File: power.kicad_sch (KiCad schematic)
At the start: 33 parts, among them J5 Conn_01x02, Q1 2N7002K, Q2 CSD17311Q5, Q3 CSD17311Q5, U10 DS4432U+, U13 TPS40305, U9 INA260

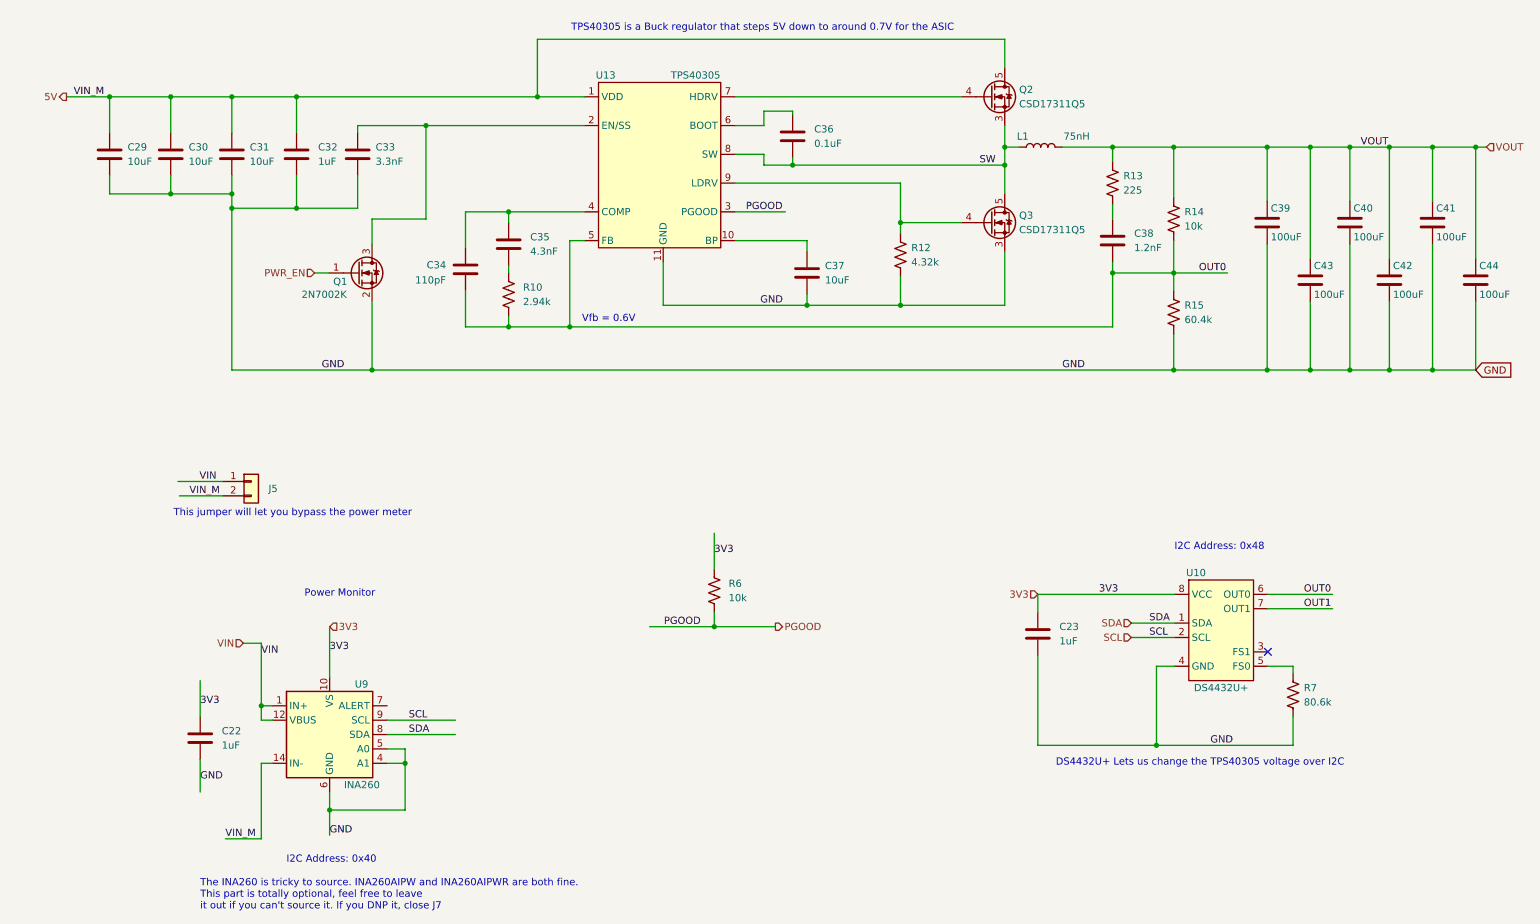
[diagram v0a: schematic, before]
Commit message: adding logo and docs
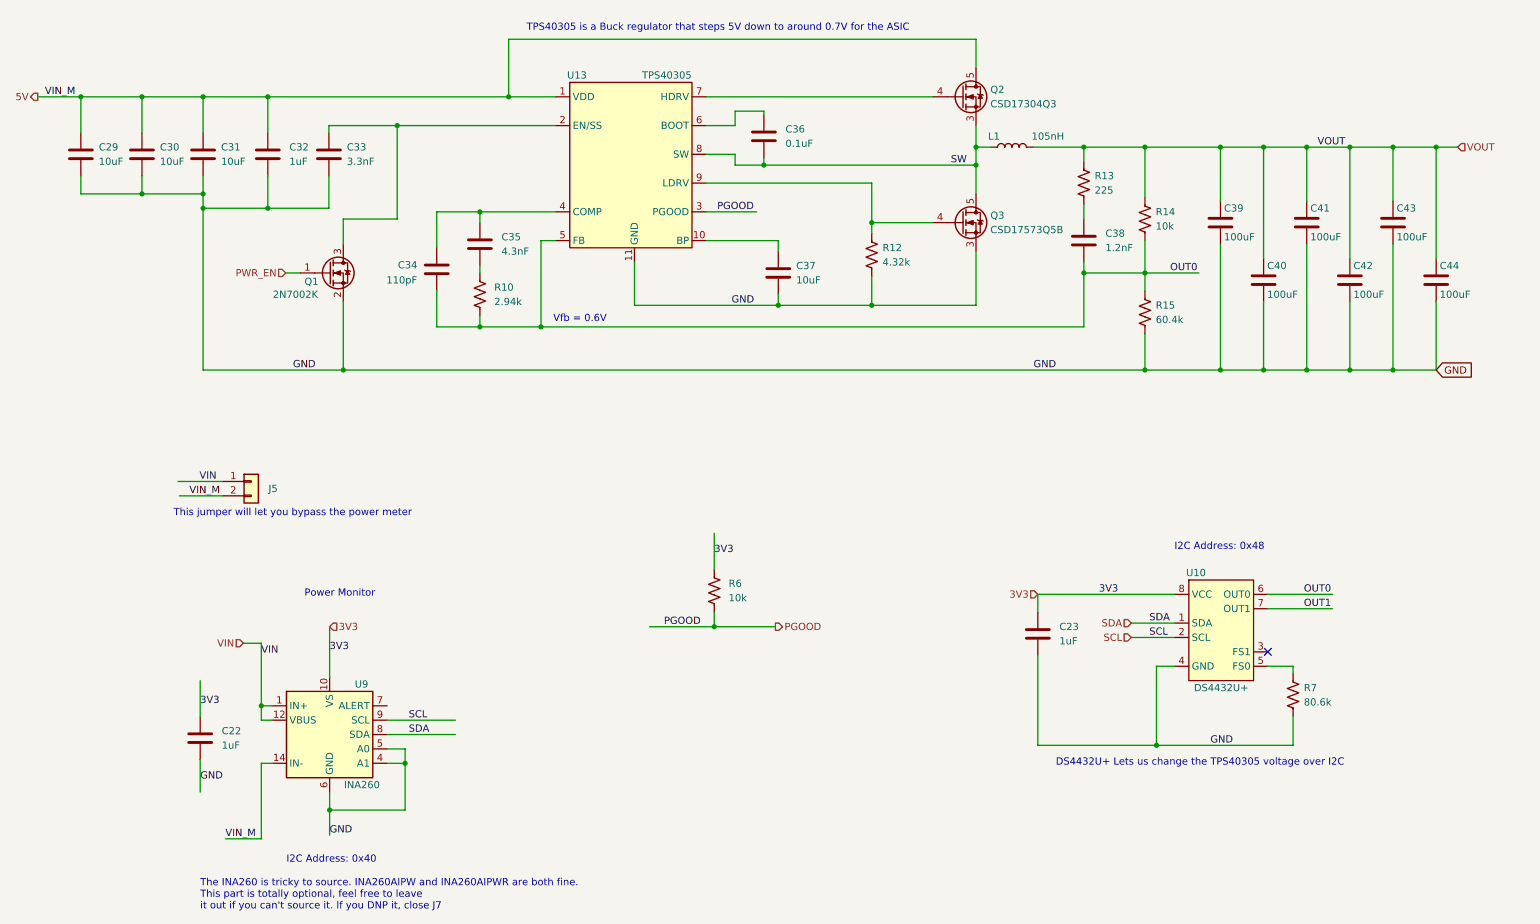
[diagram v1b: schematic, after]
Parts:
- C29, C30, C31: DK (none) -> 399-C0805C106K8PAC7800DKR-ND; PARTNO (none) -> C0805C106K8PAC7800
- C37: DK 1276-1096-1-ND -> 399-C0805C106K8PAC7800DKR-ND; PARTNO CL21A106KOQNNNE -> C0805C106K8PAC7800
- C39, C40, C41, C42, C43, C44: footprint Capacitor_SMD:C_1206_3216Metric -> Capacitor_SMD:C_1210_3225Metric; DK 445-6008-1-ND -> C1210C107M9PAC7800; PARTNO C3216X5R0J107M160AB -> C1210C107M9PACTU
- L1: value 75nH -> 105nH; DK (none) -> 283-FP0705R1-R10-RCT-ND; PARTNO (none) -> FP0705R1-R10-R
- Q2: value CSD17311Q5 -> CSD17304Q3; DK (none) -> 296-27509-1-ND; PARTNO (none) -> CSD17304Q3
- Q3: value CSD17311Q5 -> CSD17573Q5B; DK (none) -> 296-39836-1-ND; PARTNO (none) -> CSD17573Q5B
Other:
- moved on the sheet: C29, C30, C31, C32, C33, C34, C35, C36, C37, C38, C39, L1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

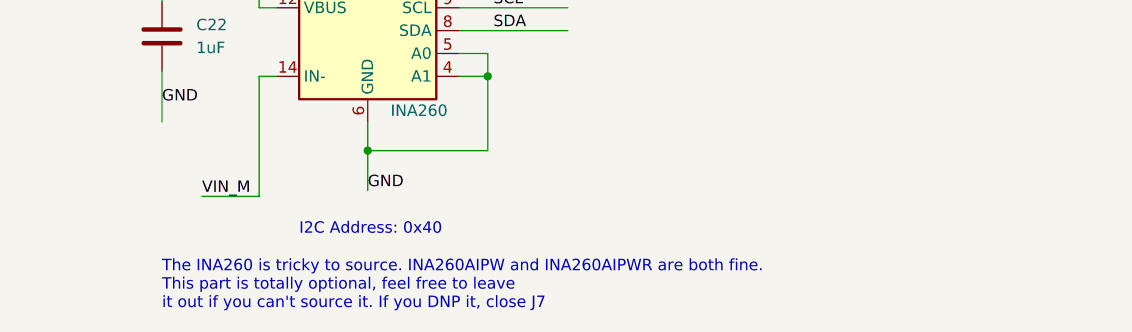
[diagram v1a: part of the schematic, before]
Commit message: migrated over lots of bitaxe parts to blockaxe
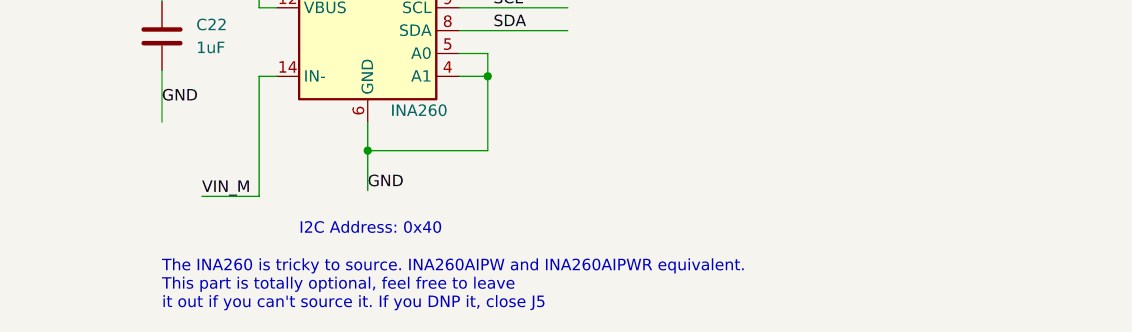
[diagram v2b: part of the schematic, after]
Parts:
- L1: footprint bitaxe:FP1005R1-R15-R -> blockaxe:FP1005R1-R15-R
- Q2: footprint bitaxe:CSD17311Q5 -> (none); symbol bitaxe:Q_NMOS_CSD17311Q5_1 -> blockaxe:Q_NMOS_CSD17311Q5_1; DK 296-27509-1-ND -> 296-39836-1-ND; PARTNO CSD17304Q3 -> CSD17573Q5B
- Q3: footprint bitaxe:CSD17311Q5 -> (none); symbol bitaxe:Q_NMOS_CSD17311Q5_1 -> blockaxe:Q_NMOS_CSD17311Q5_1
- U10: symbol bitaxe:DS4432U+ -> blockaxe:DS4432U+
- U13: footprint bitaxe:TPS40305 -> blockaxe:TPS40305; symbol bitaxe:TPS40305 -> blockaxe:TPS40305
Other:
- note added: "The INA260 is tricky to source. INA260AIPW and INA260AIPWR equivalent. This part is totally optional, feel free to leave it out if you can't source it. If you DNP it, close J5"
- note removed: "The INA260 is tricky to source. INA260AIPW and INA260AIPWR are both fine. This part is totally optional, feel free to leave it out if you can't source it. If you DNP it, close J7"
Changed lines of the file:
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@@
     (effects (font (size 1.27 1.27)) (justify left bottom))
   )
-  (text "The INA260 is tricky to source. INA260AIPW and INA260AIPWR are both fine.\nThis part is totally optional, feel free to leave \nit out if you can't source it. If you DNP it, close J7"
+  (text "The INA260 is tricky to source. INA260AIPW and INA260AIPWR equivalent.\nThis part is totally optional, feel free to leave \nit out if you can't source it. If you DNP it, close J5"
     (at 50.927 178.689 0)
     (effects (font (size 1.27 1.27)) (justify left bottom))
@@
     (effects (font (size 1.27 1.27)) (justify right))
   )
-  (symbol (lib_id "bitaxe:DS4432U+") (at 231.902 129.159 0) (unit 1)
+  (symbol (lib_id "blockaxe:DS4432U+") (at 231.902 129.159 0) (unit 1)
     (in_bom yes) (on_board yes) (dnp no)
     (property "Reference" "U10" (at 226.822 118.999 0)
@@
     )
   )
-  (symbol (lib_id "bitaxe:Q_NMOS_CSD17311Q5_1") (at 185.42 57.15 0) (unit 1)
+  (symbol (lib_id "blockaxe:Q_NMOS_CSD17311Q5_1") (at 185.42 57.15 0) (unit 1)
     (in_bom yes) (on_board yes) (dnp no)
     (property "Reference" "Q3" (at 190.5 55.88 0)
@@
       (effects (font (size 1.27 1.27)) (justify left))
     )
-    (property "Footprint" "bitaxe:CSD17311Q5" (at 190.5 54.61 0)
+    (property "Footprint" "" (at 190.5 54.61 0)
       (effects (font (size 1.27 1.27)) hide)
     )
@@
     )
   )
-  (symbol (lib_id "bitaxe:Q_NMOS_CSD17311Q5_1") (at 185.42 34.925 0) (unit 1)
+  (symbol (lib_id "blockaxe:Q_NMOS_CSD17311Q5_1") (at 185.42 34.925 0) (unit 1)
     (in_bom yes) (on_board yes) (dnp no)
     (property "Reference" "Q2" (at 190.5 33.655 0)
@@
       (effects (font (size 1.27 1.27)) (justify left))
     )
-    (property "Footprint" "bitaxe:CSD17311Q5" (at 190.5 32.385 0)
+    (property "Footprint" "" (at 190.5 32.385 0)
       (effects (font (size 1.27 1.27)) hide)
     )
@@
       (effects (font (size 1.27 1.27)) hide)
     )
-    (property "DK" "296-27509-1-ND" (at 185.42 34.925 0)
-      (effects (font (size 1.27 1.27)) hide)
-    )
-    (property "PARTNO" "CSD17304Q3" (at 185.42 34.925 0)
+    (property "DK" "296-39836-1-ND" (at 185.42 34.925 0)
+      (effects (font (size 1.27 1.27)) hide)
+    )
+    (property "PARTNO" "CSD17573Q5B" (at 185.42 34.925 0)
       (effects (font (size 1.27 1.27)) hide)
     )
@@
       (effects (font (size 1.27 1.27)))
     )
-    (property "Footprint" "bitaxe:FP1005R1-R15-R" (at 194.31 43.815 0)
+    (property "Footprint" "blockaxe:FP1005R1-R15-R" (at 194.31 43.815 0)
       (effects (font (size 1.27 1.27)) hide)
     )
@@
     )
   )
-  (symbol (lib_id "bitaxe:TPS40305") (at 127.635 47.625 0) (unit 1)
+  (symbol (lib_id "blockaxe:TPS40305") (at 127.635 47.625 0) (unit 1)
     (in_bom yes) (on_board yes) (dnp no)
     (property "Reference" "U13" (at 117.475 31.115 0)
@@
       (effects (font (size 1.27 1.27)))
     )
-    (property "Footprint" "bitaxe:TPS40305" (at 113.665 59.055 0)
-      (effects (font (size 1.27 1.27)) hide)
-    )
+    (property "Footprint" "blockaxe:TPS40305" (at 113.665 59.055 0)
+      (effects (font (size 1.27 1.27)) hide)
+    )

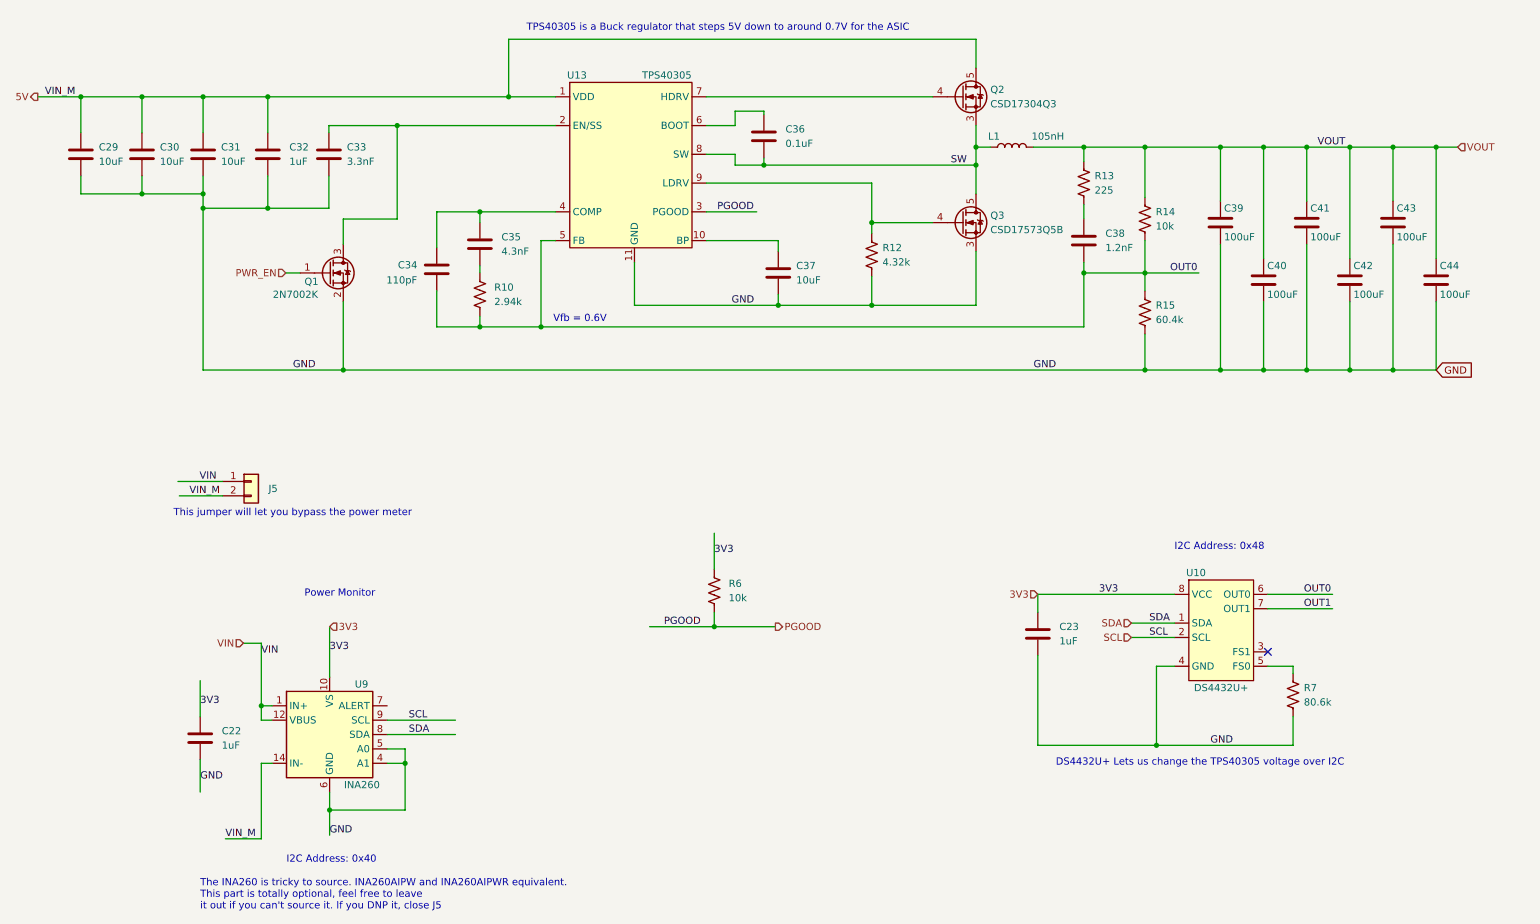
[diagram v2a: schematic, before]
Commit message: switched to the LM27402 buck regulator
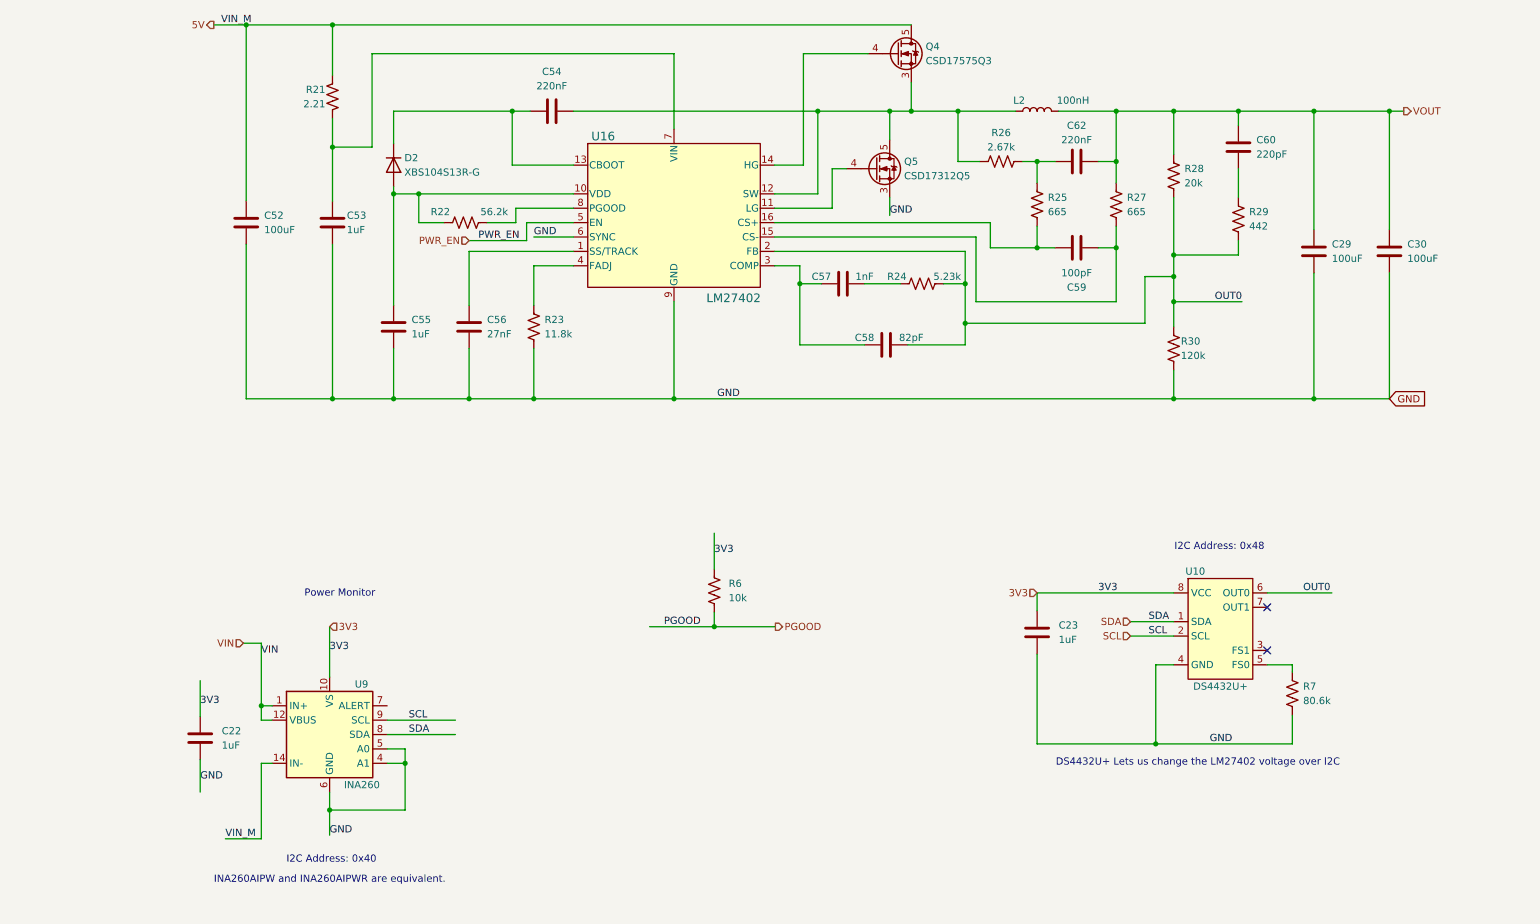
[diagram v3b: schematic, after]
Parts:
- removed C31, C37: 10uF, Capacitor_SMD:C_0805_2012Metric, symbol Device:C
- removed C32: 1uF, Capacitor_SMD:C_0805_2012Metric, symbol Device:C
- removed C33: 3.3nF, Capacitor_SMD:C_0402_1005Metric, symbol Device:C
- removed C34: 110pF, Capacitor_SMD:C_0402_1005Metric, symbol Device:C
- removed C35: 4.3nF, Capacitor_SMD:C_0201_0603Metric, symbol Device:C
- removed C36: 0.1uF, Capacitor_SMD:C_0402_1005Metric, symbol Device:C
- removed C38: 1.2nF, Capacitor_SMD:C_0805_2012Metric, symbol Device:C
- removed C39, C40, C41, C42, C43, C44: 100uF, Capacitor_SMD:C_1210_3225Metric, symbol Device:C
- removed J5: Conn_01x02, Connector_PinHeader_2.54mm:PinHeader_1x02_P2.54mm_Vertical, symbol Connector_Generic:Conn_01x02
- removed L1: 105nH, blockaxe:FP1005R1-R15-R, symbol Device:L
- removed Q1: 2N7002K, Package_TO_SOT_SMD:SOT-323_SC-70, symbol Transistor_FET:2N7002K
- removed Q2: CSD17304Q3, symbol blockaxe:Q_NMOS_CSD17311Q5_1
- removed Q3: CSD17573Q5B, symbol blockaxe:Q_NMOS_CSD17311Q5_1
- removed R10: 2.94k, Resistor_SMD:R_0402_1005Metric, symbol Device:R_US
- removed R12: 4.32k, Resistor_SMD:R_0402_1005Metric, symbol Device:R_US
- removed R13: 225, Resistor_SMD:R_0402_1005Metric, symbol Device:R_US
- removed R14: 10k, Resistor_SMD:R_0402_1005Metric, symbol Device:R_US
- removed R15: 60.4k, Resistor_SMD:R_0402_1005Metric, symbol Device:R_US
- removed U13: TPS40305, blockaxe:TPS40305, symbol blockaxe:TPS40305
- added C52: 100uF, Capacitor_SMD:C_1210_3225Metric, symbol Device:C
- added C53: 1uF, Capacitor_SMD:C_0805_2012Metric, symbol Device:C
- added C54: 220nF, Capacitor_SMD:C_0603_1608Metric, symbol Device:C
- added C55: 1uF, Capacitor_SMD:C_0201_0603Metric, symbol Device:C
- added C56: 27nF, Capacitor_SMD:C_0402_1005Metric, symbol Device:C
- added C57: 1nF, Capacitor_SMD:C_0805_2012Metric, symbol Device:C
- added C58: 82pF, Capacitor_SMD:C_0805_2012Metric, symbol Device:C
- added C59: 100pF, Capacitor_SMD:C_0402_1005Metric, symbol Device:C
- added C60: 220pF, Capacitor_SMD:C_0805_2012Metric, symbol Device:C
- added C62: 220nF, Capacitor_SMD:C_0402_1005Metric, symbol Device:C
- added D2: XBS104S13R-G, Diode_SMD:D_SOD-323, symbol Device:D
- added L2: 100nH, blockaxe:FP0805R1-R10-R, symbol Device:L
- added Q4: CSD17575Q3, blockaxe:DQG0008A, symbol blockaxe:Q_NMOS_CSD17311Q5_1
- added Q5: CSD17312Q5, symbol blockaxe:Q_NMOS_CSD17311Q5_1
- added R21: 2.21, Resistor_SMD:R_0402_1005Metric, symbol Device:R_US
- added R22: 56.2k, Resistor_SMD:R_0402_1005Metric, symbol Device:R_US
- added R23: 11.8k, Resistor_SMD:R_0402_1005Metric, symbol Device:R_US
- added R24: 5.23k, Resistor_SMD:R_0402_1005Metric, symbol Device:R_US
- added R25, R27: 665, Resistor_SMD:R_0402_1005Metric, symbol Device:R_US
- added R26: 2.67k, Resistor_SMD:R_0402_1005Metric, symbol Device:R_US
- added R28: 20k, Resistor_SMD:R_0402_1005Metric, symbol Device:R_US
- added R29: 442, Resistor_SMD:R_0402_1005Metric, symbol Device:R_US
- added R30: 120k, Resistor_SMD:R_0402_1005Metric, symbol Device:R_US
- added U16: LM27402, blockaxe:SQB16A, symbol blockaxe:LM27402SQ_NOPB
- C29, C30: value 10uF -> 100uF; footprint Capacitor_SMD:C_0805_2012Metric -> Capacitor_SMD:C_1210_3225Metric; DK 399-C0805C106K8PAC7800DKR-ND -> 490-9969-1-ND; PARTNO C0805C106K8PAC7800 -> GRM32ER61A107ME20L
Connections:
- net 5V: now also C52.1, Q4.5 (D), R21.1; no longer C29.1, C30.1
- net OUT0: now also C58.2, R24.2, R28.2, R29.2, R30.1, U16.2 (FB)
- net PWR_EN: now also U16.5 (EN)
- net VOUT: now also C29.1, C30.1, C60.1, C62.2, L2.2, R27.1, R28.1
- net GND renamed PAD
- net PAD: now also C52.2, C53.2, C55.2, C56.2, Q5.1, Q5.2, Q5.3 (S), R23.2, R30.2, U16.6 (SYNC), U16.9 (GND), U16.EP (PAD)
- net OUT1: no longer names the net of U10.7 (OUT1)
- new net: C59.1, R27.2, U16.15 (CS-)
- new net: C62.1, R25.1, R26.2
- new net: C59.2, R25.2, U16.16 (CS+)
- new net: C54.1, D2.1 (K), U16.13 (CBOOT)
- new net: C54.2, L2.1, Q4.1, Q4.2, Q4.3 (S), Q5.5 (D), R26.1, U16.12 (SW)
- new net: Q5.4 (G), U16.11 (LG)
- new net: C56.1, U16.1 (SS/TRACK)
- new net: C55.1, D2.2 (A), R22.1, U16.10 (VDD)
- new net: Q4.4 (G), U16.14 (HG)
- new net: C57.1, C58.1, U16.3 (COMP)
- new net: R23.1, U16.4 (FADJ)
- new net: C53.1, R21.2, U16.7 (VIN)
- new net: R22.2, U16.8 (PGOOD)
- new net: C57.2, R24.1
- new net: C60.2, R29.1
- no-connect marks 1 -> 2
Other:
- note added: "DS4432U+ Lets us change the LM27402 voltage over I2C"
- note added: "INA260AIPW and INA260AIPWR are equivalent."
- note removed: "DS4432U+ Lets us change the TPS40305 voltage over I2C"
- note removed: "TPS40305 is a Buck regulator that steps 5V down to around 0.7V for the ASIC"
- note removed: "The INA260 is tricky to source. INA260AIPW and INA260AIPWR equivalent. This part is totally optional, feel free to leave it out if you can't source it. If you DNP it, close J5"
- note removed: "This jumper will let you bypass the power meter"
- note removed: "Vfb = 0.6V"
